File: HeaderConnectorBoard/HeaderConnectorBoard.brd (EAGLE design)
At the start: 39.7 x 53.3 mm, 2 parts

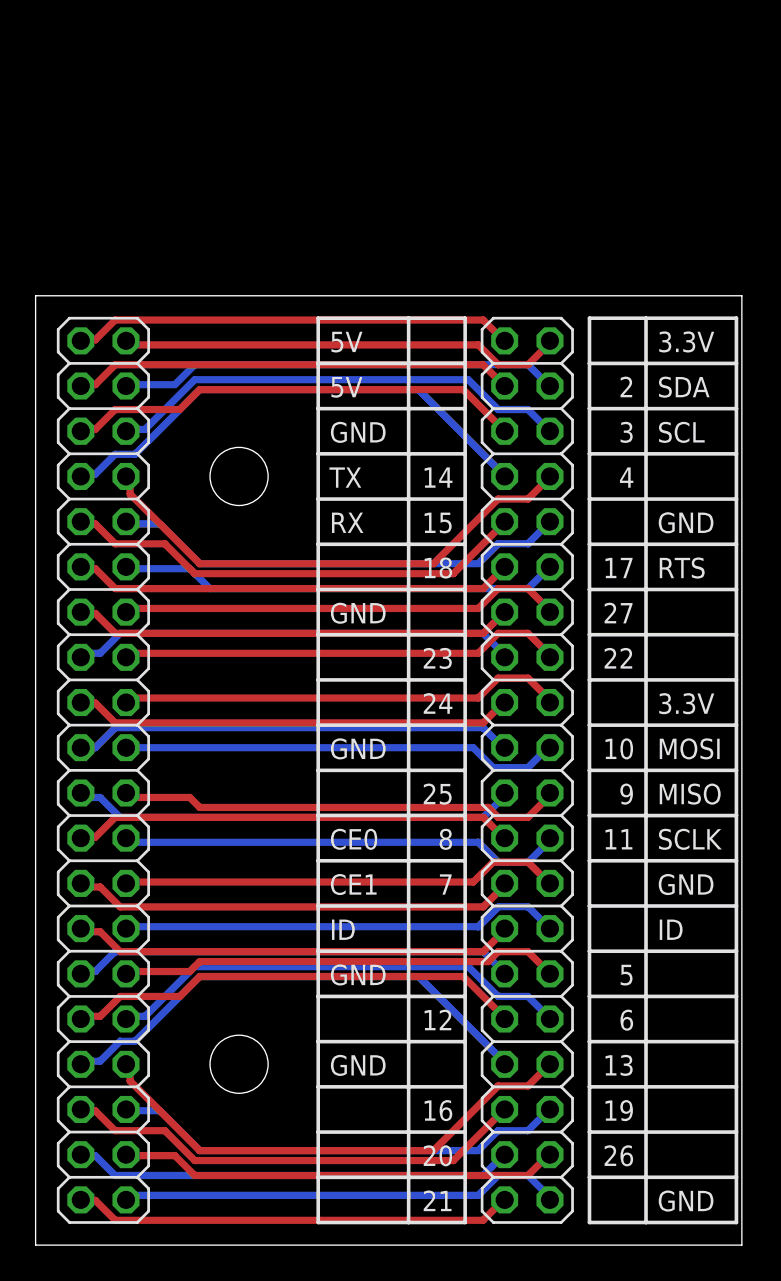
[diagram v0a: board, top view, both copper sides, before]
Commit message: lid connector - changed size and mounting for top mounting on lid
New connector board will be mounted on top (used to be bottom) of RaspberrySTEM
Lid, with an extra arcrylic spacer in between.
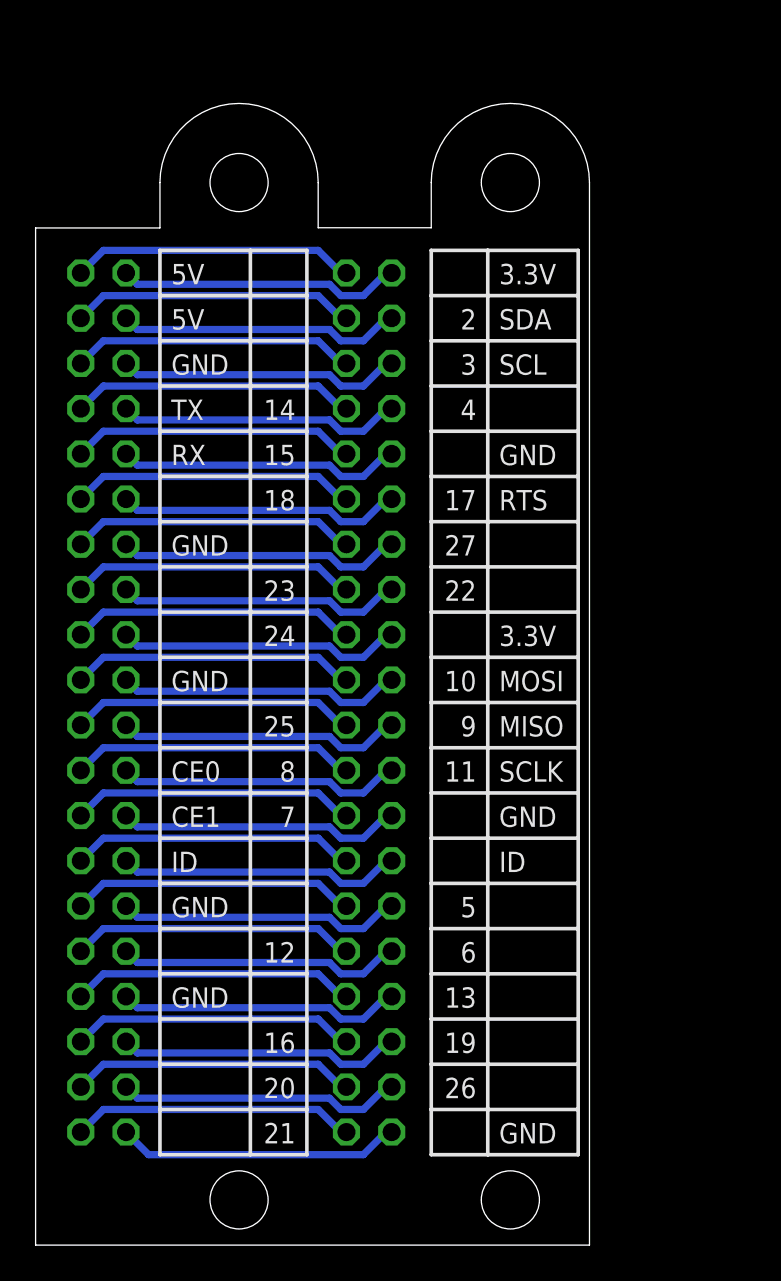
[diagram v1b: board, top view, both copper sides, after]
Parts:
- moved JP1 9.67 mm to (18.7, 30.5)
- moved JP2 3.81 mm to (3.81, 30.5)
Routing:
- net 14/TX: track 28.4 -> 16.0 mm
- net GND7: track 28.3 -> 16.0 mm
- net 13: track 27.9 -> 16.0 mm
- net 4: track 27.8 -> 16.0 mm
- net 12: track 26.2 -> 16.0 mm
- net GND: track 26.2 -> 16.0 mm
- net GND5: track 26.2 -> 16.0 mm
- net 19: track 26.2 -> 16.0 mm
- net 6: track 25.8 -> 16.0 mm
- net 15/RX: track 25.8 -> 16.0 mm
- net 3/SCL: track 25.7 -> 16.0 mm
- net 16: track 25.7 -> 16.0 mm
- net 9/MISO: track 25.0 -> 16.0 mm
- net 24: track 25.0 -> 16.0 mm
- net 21: track 25.0 -> 16.0 mm
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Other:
- board size 39.7 x 53.3 mm -> 31.1 x 64.1 mm

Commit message: lic connector - adjustments to fit with acrylic
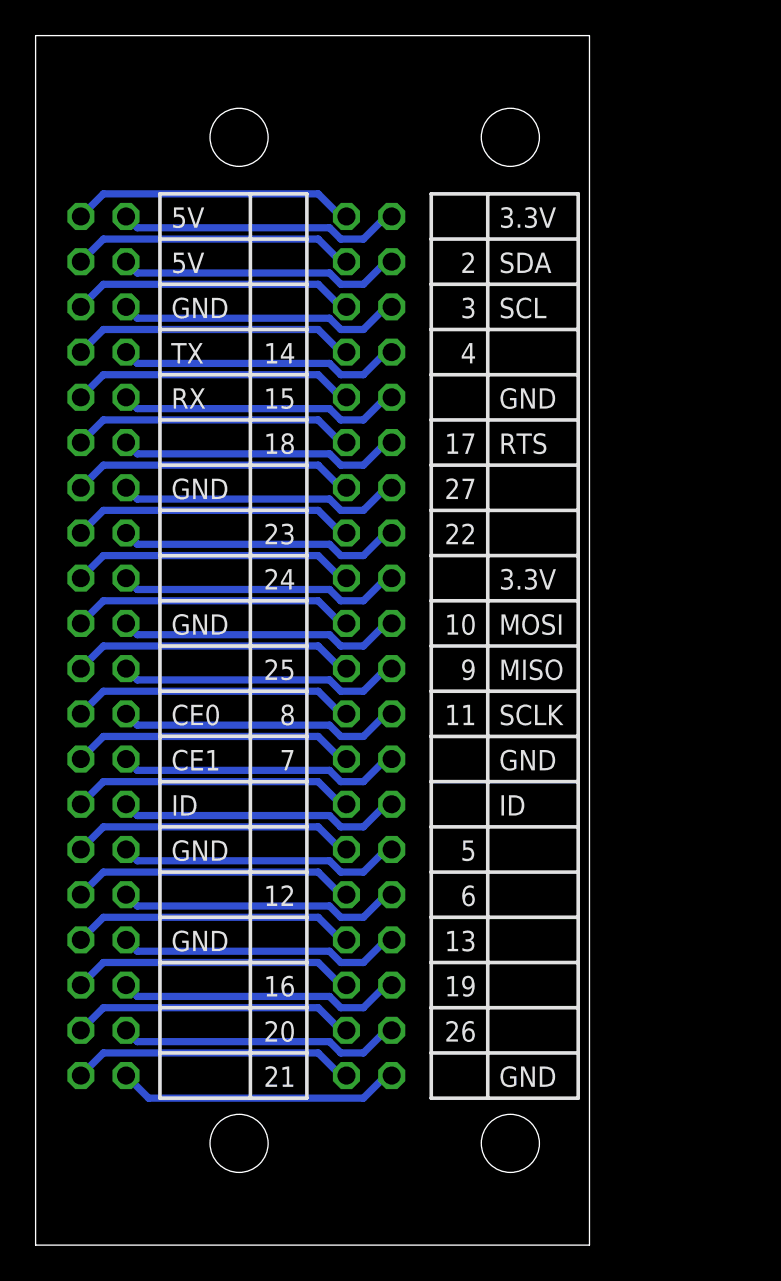
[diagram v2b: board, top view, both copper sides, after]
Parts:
- moved JP1 3.18 mm to (18.7, 33.7)
- moved JP2 3.18 mm to (3.81, 33.7)
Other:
- board size 31.1 x 64.1 mm -> 31.1 x 67.9 mm
